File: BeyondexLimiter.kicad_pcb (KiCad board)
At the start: 2 copper layers, 22.5 x 13 mm, 9 parts, among them U1 CN5711

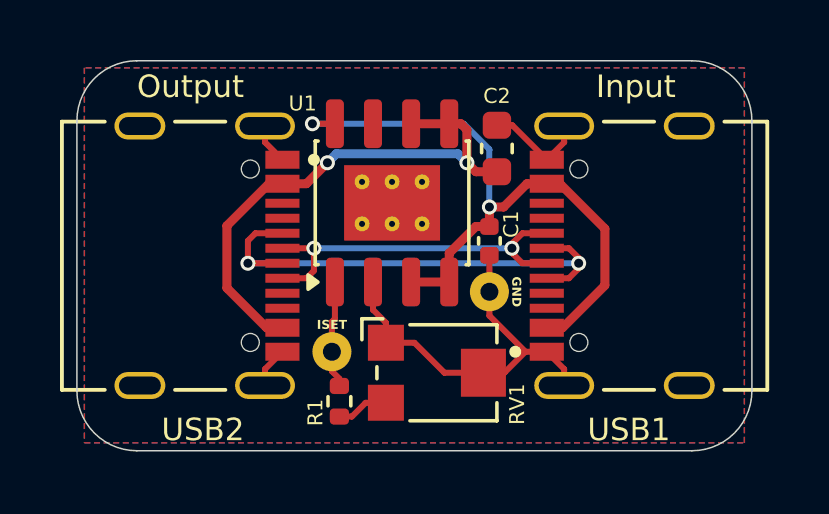
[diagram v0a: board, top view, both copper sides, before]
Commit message: Fix wrong footprint for R1, rearrange a little
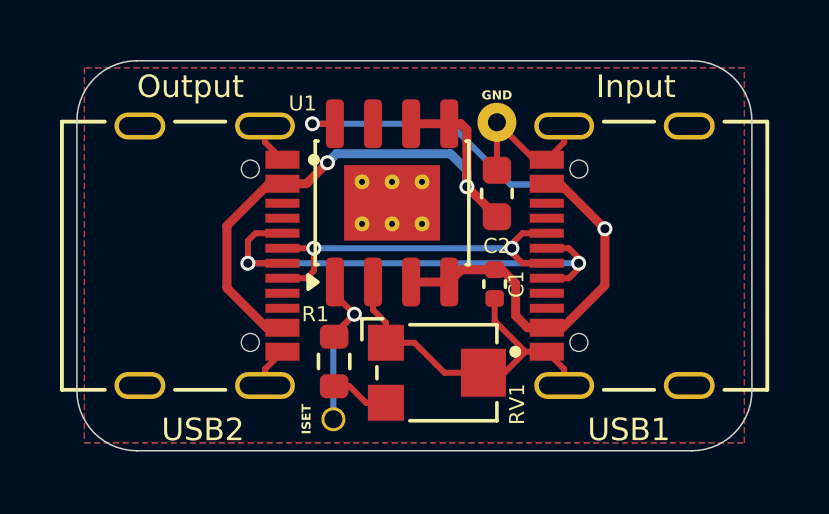
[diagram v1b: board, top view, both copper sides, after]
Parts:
- R1: footprint Resistor_SMD:R_0402_1005Metric -> Resistor_SMD:R_0603_1608Metric
- TP1: footprint BeyondexLimiter:TestPoint_Plated_Hole_D0.6mm -> BeyondexLimiter:TestPoint_Plated_Hole_D0.6mm_Asymmetric
- moved TP2 5.66 mm to (171.5, 93.0), turned to 0 degrees
- moved TP1 2.25 mm to (166.1, 103.0), turned to 90 degrees
- moved C2 1.50 mm to (171.5, 95.4)
- moved C1 1.45 mm to (171.4, 98.4)
- moved R1 1.34 mm to (166.1, 101.0)
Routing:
- net /ISET: track 3.61 -> 6.16 mm, vias 0 -> 1
- net /VIN: track 22.7 -> 25.0 mm
- net /VOUT: track 17.8 -> 19.5 mm
